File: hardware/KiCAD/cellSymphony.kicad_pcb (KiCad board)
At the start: 2 copper layers, 56.5 x 151 mm, 11 parts, among them SW1 RotaryEncoder_Switch, SW2 RotaryEncoder_Switch, SW3 RotaryEncoder_Switch, SW4 RotaryEncoder_Switch, SW5 RotaryEncoder_Switch, U1 Raspberry Pi Zero 2 W

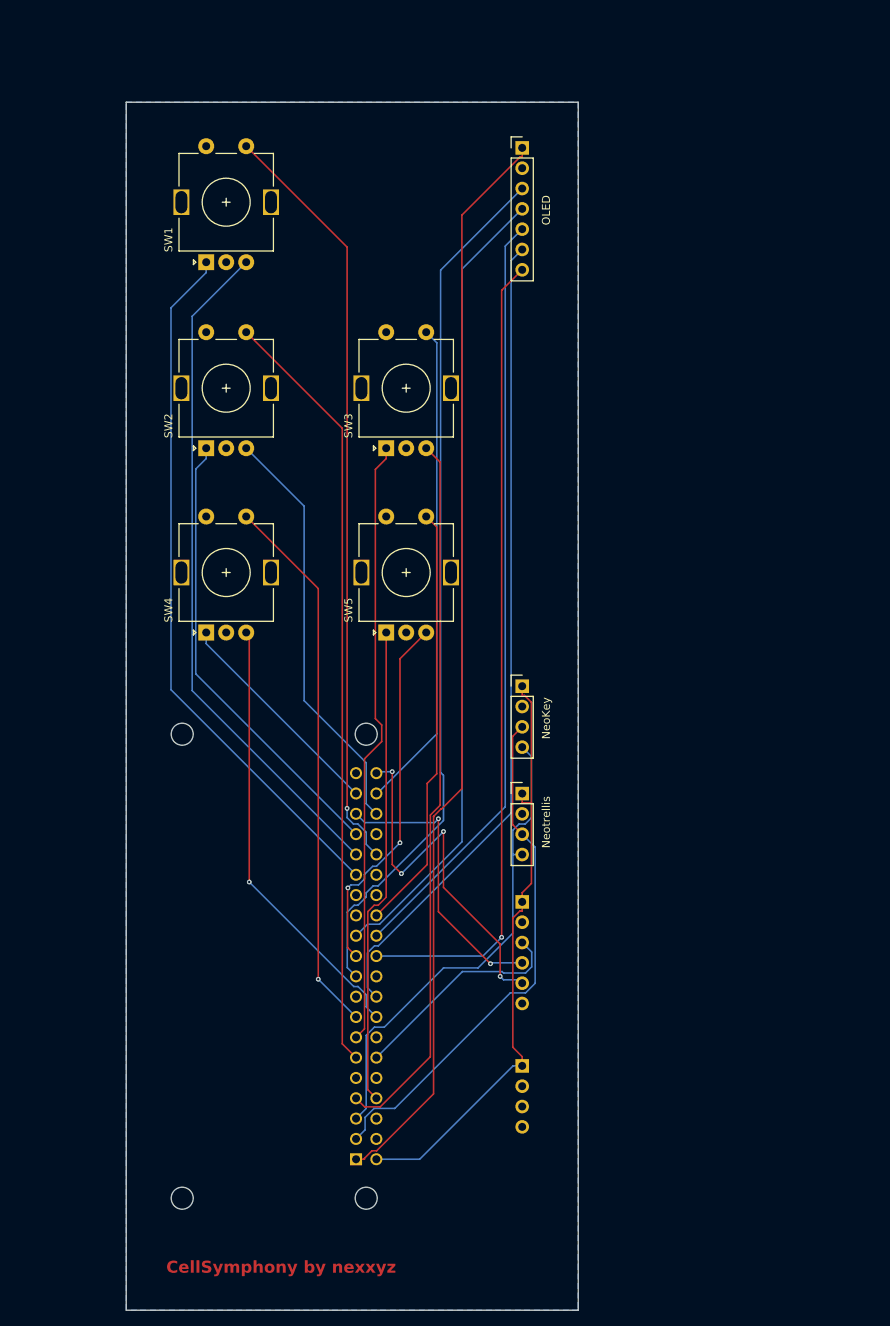
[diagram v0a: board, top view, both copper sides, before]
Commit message: hardware: add new PCB revision with KiCAD libs and reports
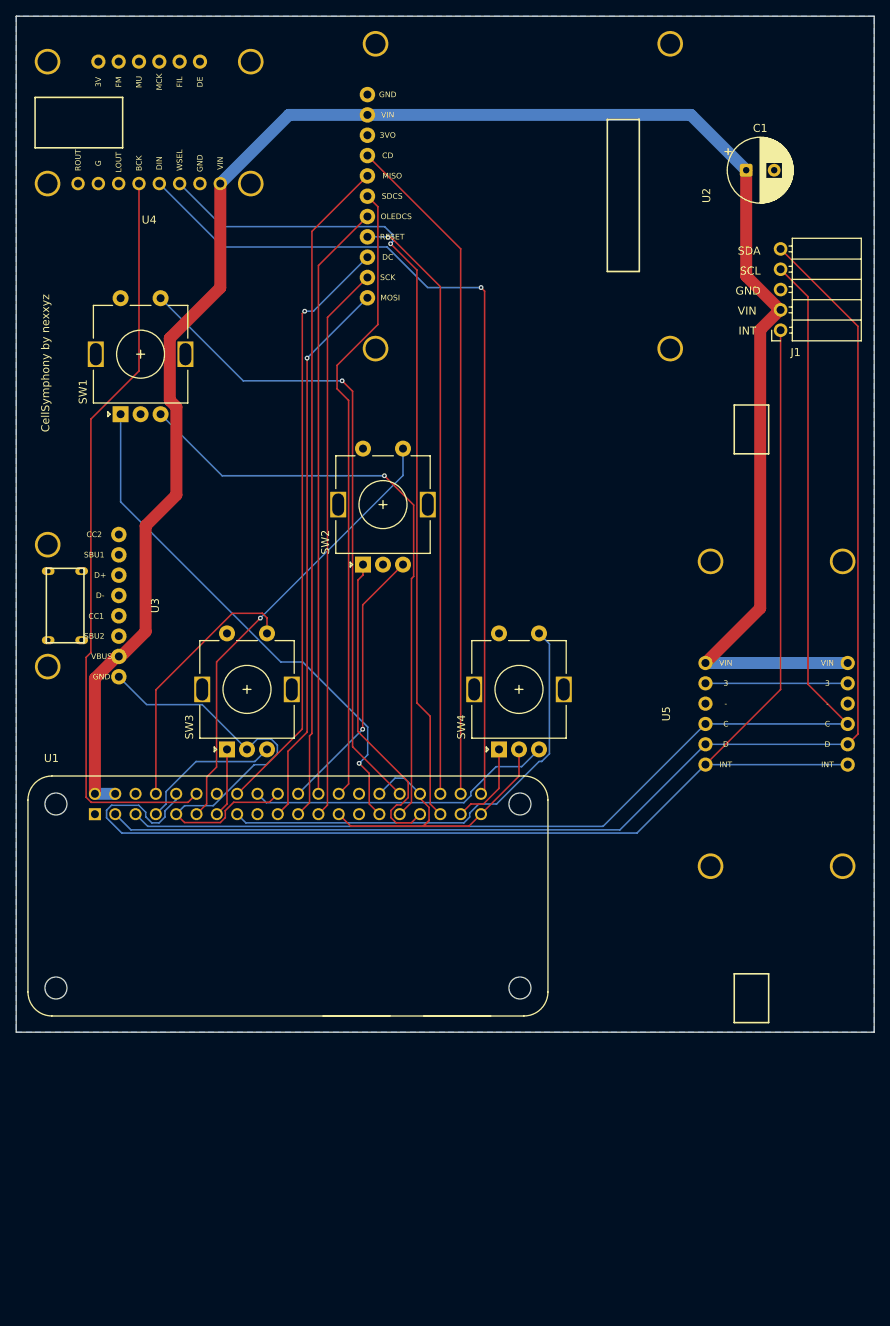
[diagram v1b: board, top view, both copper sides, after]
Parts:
- removed ADA4090, NeoKey, Neotrellis: Conn_01x04, Connector_PinHeader_2.54mm:PinHeader_1x04_P2.54mm_Vertical
- removed ADA6250: Conn_01x06, Connector_PinHeader_2.54mm:PinHeader_1x06_P2.54mm_Vertical
- removed OLED: Conn_01x07, Connector_PinHeader_2.54mm:PinHeader_1x07_P2.54mm_Vertical
- removed SW5: RotaryEncoder_Switch, Rotary_Encoder:RotaryEncoder_Alps_EC11E-Switch_Vertical_H20mm
- added C1: 470uf, Capacitor_THT:CP_Radial_D8.0mm_P3.50mm, F.Cu at (105.5, 34.0)
- added J1: NeoTrellis_Conn, adafruit-modules:Adafruit_NeoTrellis_Connector_1x5, F.Cu at (121.3, 44.0)
- added U2: SSD1351, adafruit-modules:Adafruit_SSD1351_OLED, F.Cu at (98.5, 15.7)
- added U3: USB-C, adafruit-modules:Adafruit_USB_C_Breakout, F.Cu at (29.6, 78.3)
- added U4: PCM5102a, adafruit-modules:Adafruit_PCM510x_I2S_DAC_6250, F.Cu at (46.1, 38.2)
- added U5: NeoKey, adafruit-modules:Adafruit_NeoKey_1x4_QT, F.Cu at (98.5, 140.1)
- U1: value Raspberry Pi Zero 2 W -> Raspberry Zero 2 W; moved to F.Cu
- moved SW3 42.6 mm to (40.6, 106.4)
- moved SW4 39.4 mm to (74.6, 106.4)
- moved SW2 24.4 mm to (57.6, 83.3)
- moved SW1 21.8 mm to (27.3, 64.5)
- moved U1 8.94 mm to (48.2, 124.7), turned to 0 degrees
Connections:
- SW2 pad B: Net-(U1-GPIO16) -> Net-(U1-GPIO25/GPIO_GEN6)
- SW3 pad S1: Net-(U1-GPIO20) -> Net-(U1-GPIO14/TXD0)
- SW4 pad B: Net-(U1-GPIO23/GPIO_GEN4) -> Net-(U1-GPIO24/GPIO_GEN5)
- U1 pad 1: Net-(OLED1-VIN) -> unconnected-(U1-3V3_1-Pad1)
- U1 pad 10: unconnected-(U1-GPIO15/RXD0-Pad10) -> Net-(J1-INT)
- U1 pad 14: unconnected-(U1-GND_14-Pad14) -> GND
- U1 pad 18: Net-(OLED1-DC) -> Net-(U1-GPIO24/GPIO_GEN5)
- U1 pad 20: unconnected-(U1-GND_20-Pad20) -> GND
- U1 pad 22: Net-(OLED1-RST) -> Net-(U1-GPIO25/GPIO_GEN6)
- U1 pad 25: unconnected-(U1-GND_25-Pad25) -> GND
- U1 pad 30: unconnected-(U1-GND_30-Pad30) -> GND
- U1 pad 34: unconnected-(U1-GND_34-Pad34) -> GND
- U1 pad 39: unconnected-(U1-GND_39-Pad39) -> GND
- U1 pad 4: unconnected-(U1-5V_4-Pad4) -> +5V
- U1 pad 9: unconnected-(U1-GND_9-Pad9) -> GND
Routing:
- net Net-(J1-INT): track 0.00 -> 168.7 mm
- net +5V: track 75.1 -> 243.5 mm
- net Net-(OLED1-VIN): track 136.2 -> 0.00 mm
- net Net-(OLED1-DC): track 102.2 -> 0.00 mm
- net Net-(OLED1-RST): track 101.1 -> 0.00 mm, vias 1 -> 0
- net Net-(J1-SDA): track 65.1 -> 163.3 mm
- net GND: track 0.00 -> 97.9 mm
- net Net-(J1-SCL): track 60.9 -> 155.3 mm
- net Net-(U1-GPIO4/GPIO_GCLK): track 89.6 -> 18.2 mm
- net Net-(U1-GPIO19): track 35.8 -> 104.4 mm, vias 2 -> 1
- net Net-(U1-GPIO27/GPIO_GEN2): track 75.9 -> 8.62 mm
- net Net-(U1-GPIO18/GPIO_GEN1): track 27.8 -> 94.0 mm
- net Net-(U1-GPIO21): track 46.9 -> 109.3 mm, vias 4 -> 1
- net Net-(U1-GPIO17/GPIO_GEN0): track 96.4 -> 56.4 mm, vias 0 -> 1
- net Net-(U1-GPIO10/SPI_MOSI): track 108.9 -> 69.2 mm, vias 0 -> 1
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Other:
- board size 56.5 x 151 mm -> 107.2 x 127 mm
